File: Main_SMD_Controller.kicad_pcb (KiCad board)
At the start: 4 copper layers, 65 x 85 mm, 59 parts, among them J1 2.1-5.5 +12VDC, J10 Vin_-, J11 Conn_01x02, J12 Vsens, J13 Vin+, J2 Switch_Control, J3 +5V, J4 AnalogIO, J5 +12V, J6 VsensJMP, J7 Drain, J8 Gate, J9 Source, P1 Eoshi-chan_Silk, P2 Eoshi-chan_Silk, P3 Serial_QR, Q1 2N7002K, U1 NJW4191M, U2 NJM7805SDL1, U3 TC74HC4066AP, U4 AD8226ARZ, U5 S-89713B-K8T2U

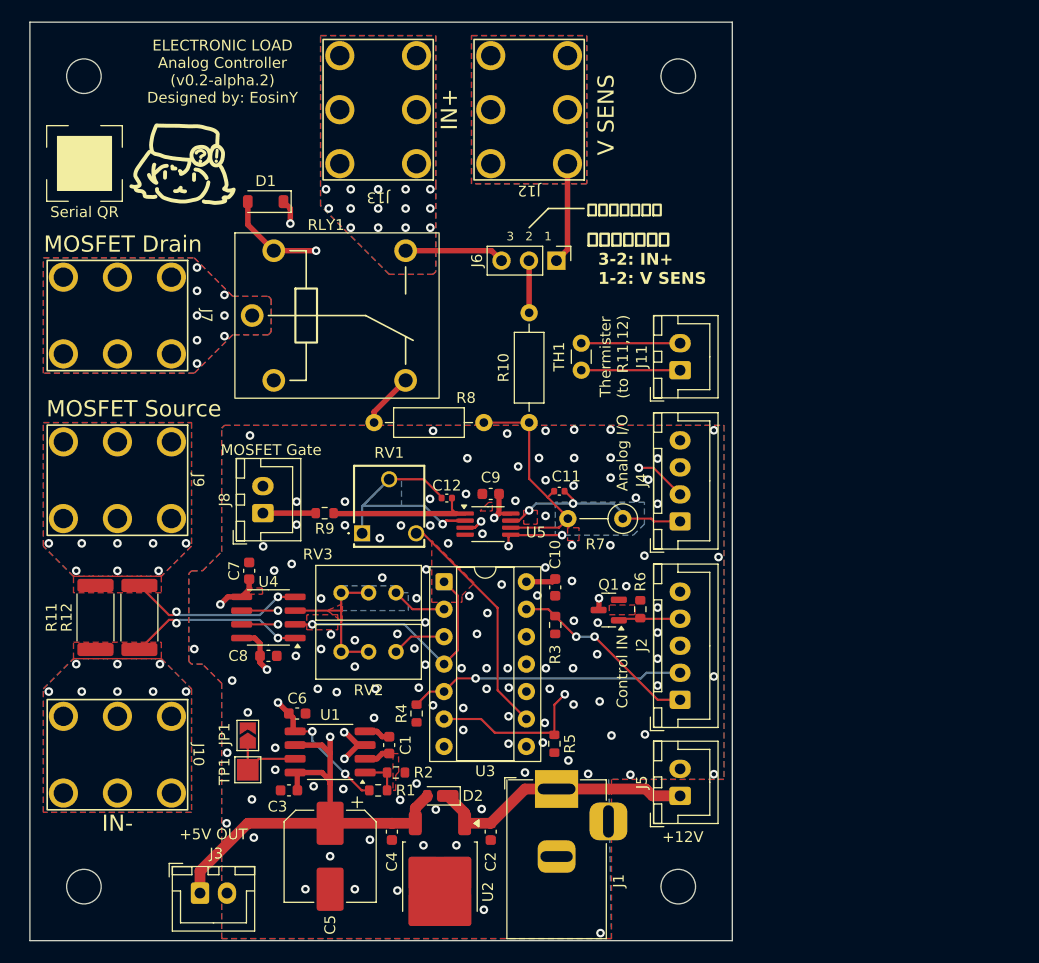
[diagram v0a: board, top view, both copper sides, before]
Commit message: 4 layered
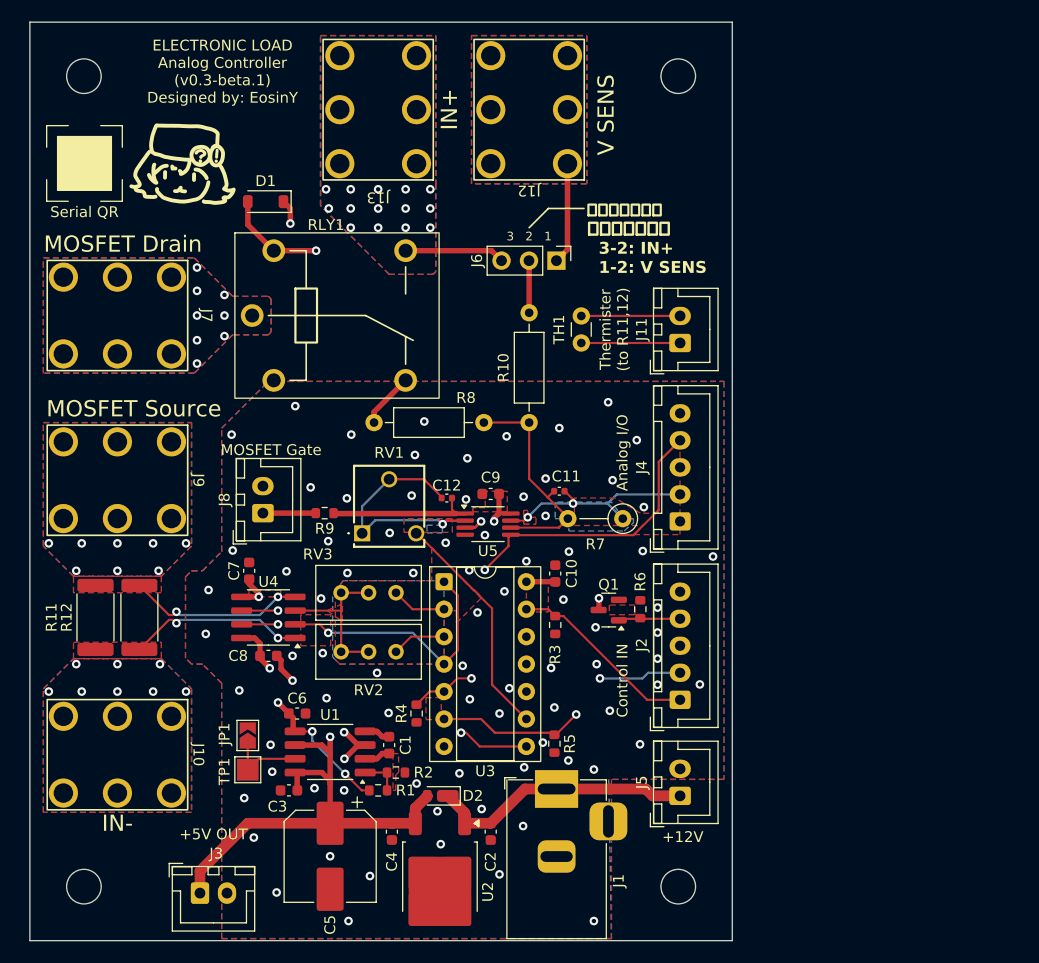
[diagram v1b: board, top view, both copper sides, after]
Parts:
- J4: footprint Connector_JST:JST_XH_B4B-XH-A_1x04_P2.50mm_Vertical -> Connector_JST:JST_XH_B5B-XH-A_1x05_P2.50mm_Vertical
- moved J11 2.52 mm to (90.2, 59.7)
- moved TH1 2.52 mm to (81.0, 59.7)
- moved C10 1.28 mm to (78.6, 81.0), turned to 90 degrees
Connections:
- J4 pad 1: /Vmeas -> /Imeas
- J4 pad 2: /Vref -> /Vmeas
- J4 pad 3: Vofs -> /Vref
- J4 pad 4: GND -> Vofs
- U3 pad 8: Net-(U3-Pad8) -> /Imeas
- U4 pad 7: Net-(U3-Pad8) -> /Imeas
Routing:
- net /Imeas: track 0.00 -> 72.2 mm, vias 0 -> 2
- net Net-(U3-Pad8): track 31.0 -> 0.00 mm, vias 1 -> 0
- net R-: track 52.3 -> 48.9 mm
- net GND: track 4.24 -> 7.13 mm, vias 123 -> 84
- net Vofs: track 47.7 -> 50.2 mm, vias 3 -> 2
- net Vconst_ENABLE: track 27.4 -> 25.8 mm
- net /Vmeas: track 19.0 -> 20.4 mm
- net VEE: track 28.3 -> 26.9 mm
- net /Vref: track 23.4 -> 22.2 mm, vias 2 -> 1
- net SHUNT_SELECT1: vias 1 -> 2
- net SHUNT_SELECT2: vias 2 -> 0
- added copper zone on In1.Cu, net GND
- added copper zone on In2.Cu, net GND
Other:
- board text added: "ELECTRONIC LOAD Analog Controller (v0.3-beta.1) Designed by: EosinY"
- board text removed: "ELECTRONIC LOAD Analog Controller (v0.2-alpha.2) Designed by: EosinY"

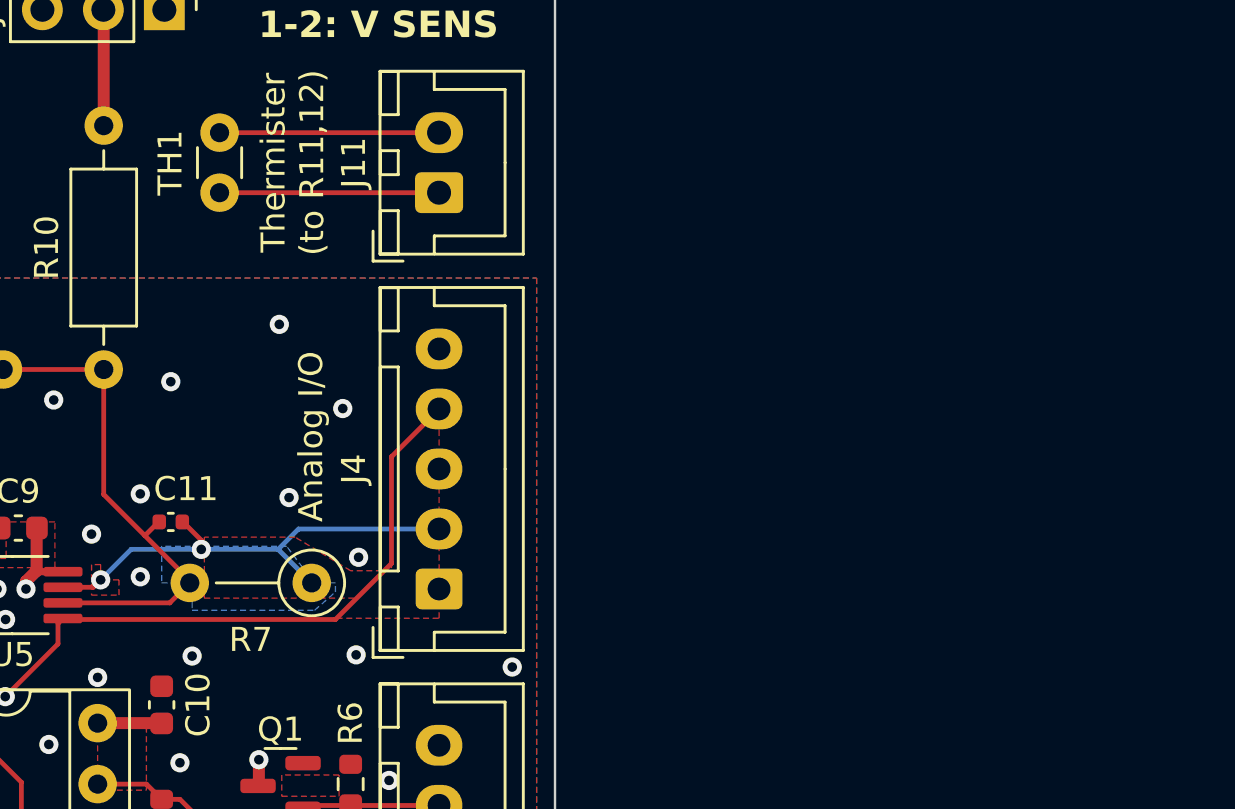
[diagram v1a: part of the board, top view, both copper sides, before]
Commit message: fix voltage measure circuit
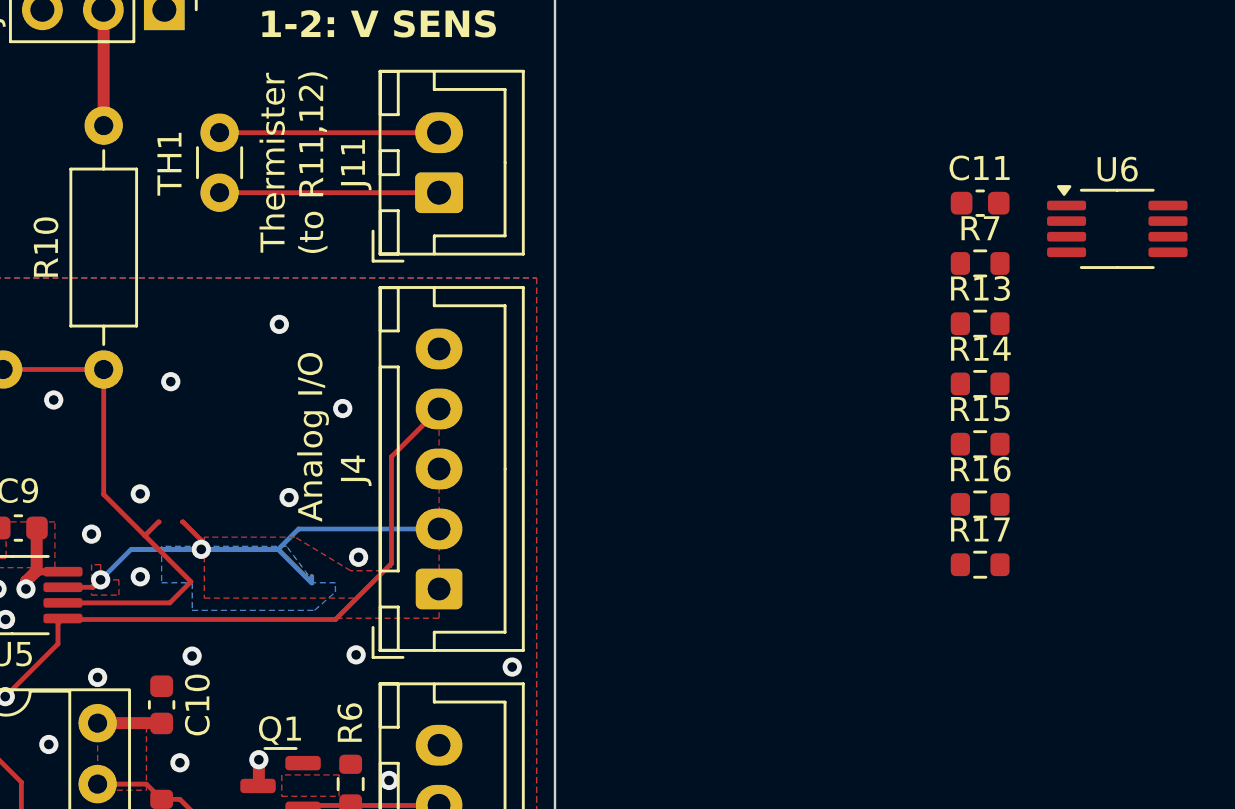
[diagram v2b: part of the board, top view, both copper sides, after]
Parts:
- added R13: 10k, Resistor_SMD:R_0603_1608Metric, F.Cu at (112.7, 65.1)
- added R14: 10k, Resistor_SMD:R_0603_1608Metric, F.Cu at (112.7, 67.7)
- added R15: 10k, Resistor_SMD:R_0603_1608Metric, F.Cu at (112.7, 70.2)
- added R16: 10k, Resistor_SMD:R_0603_1608Metric, F.Cu at (112.7, 72.7)
- added R17: 10k, Resistor_SMD:R_0603_1608Metric, F.Cu at (112.7, 75.2)
- added U6: S-89713B-K8T2U, Package_SO:MSOP-8_3x3mm_P0.65mm, F.Cu at (118.4, 61.2)
- C11: value 0.01u -> 0.1u; footprint Capacitor_SMD:C_0402_1005Metric -> Capacitor_SMD:C_0603_1608Metric
- R10: value 390k -> 150k
- R7: value 390k -> 10k; footprint Resistor_THT:R_Axial_DIN0207_L6.3mm_D2.5mm_P5.08mm_Vertical -> Resistor_SMD:R_0603_1608Metric
- moved C11 36.2 mm to (112.7, 60.1), turned to 0 degrees
- moved R7 30.9 mm to (112.7, 62.6), turned to 0 degrees
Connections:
- C11 pad 1: /Vmeas -> VCC
- C11 pad 2: Net-(C11-Pad2) -> GND
- R10 pad 1: Net-(C11-Pad2) -> Net-(R10-Pad1)
- R7 pad 1: /Vmeas -> Net-(R17-Pad2)
- R7 pad 2: Net-(C11-Pad2) -> VCC
- R8 pad 2: Net-(C11-Pad2) -> Net-(R10-Pad1)
- U5 pad 5: Vofs -> Net-(R10-Pad1)
- U5 pad 6: Net-(C11-Pad2) -> Net-(R13-Pad2)
- U5 pad 7: /Vmeas -> Net-(R13-Pad2)
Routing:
- net Net-(C11-Pad2): track 21.1 -> 0.00 mm
- net (no net): track 0.00 -> 21.1 mm

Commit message: 1733
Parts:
- moved U6 40.7 mm to (80.7, 76.4)
- moved R13 38.8 mm to (75.8, 77.1), turned to 180 degrees
- moved R15 36.4 mm to (76.6, 74.8), turned to 90 degrees
- moved R7 35.3 mm to (81.5, 79.0), turned to 180 degrees
- moved R16 33.6 mm to (79.1, 73.8)
- moved C11 32.1 mm to (85.0, 76.3), turned to -90 degrees
- moved R14 30.9 mm to (82.4, 73.8)
- moved R17 28.4 mm to (84.6, 79.0), turned to 180 degrees
- moved U5 1.55 mm to (70.8, 76.5)
- moved C9 0.16 mm to (72.5, 73.6)
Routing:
- net (no net): track 21.1 -> 0.00 mm
- net VCC: track 98.9 -> 116.1 mm
- net /Vmeas: track 20.4 -> 12.7 mm, vias 2 -> 1
- net Net-(R13-Pad1): track 0.00 -> 6.81 mm
- net Net-(R15-Pad1): track 0.00 -> 5.36 mm
- net Net-(R10-Pad1): track 0.00 -> 4.19 mm
- net Net-(R17-Pad2): track 0.00 -> 3.22 mm
- net Net-(R13-Pad2): track 0.00 -> 2.81 mm
- net GND: track 7.13 -> 9.20 mm, vias 84 -> 78
- net Net-(C12-Pad1): track 22.0 -> 20.1 mm
- net /Vref: track 22.2 -> 23.9 mm
- net Vofs: track 50.2 -> 48.6 mm
- net Net-(C12-Pad2): track 13.8 -> 12.2 mm
- net Net-(U6-Pad6): track 0.00 -> 0.65 mm

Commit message: bom and schematic pdf
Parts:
- added C13: 1u, Capacitor_SMD:C_0603_1608Metric, F.Cu at (50.2, 92.5)
- added R18: 10k, Resistor_SMD:R_0603_1608Metric, F.Cu at (53.2, 92.5)
- moved R17 2.41 mm to (82.7, 80.5)
- moved C11 1.48 mm to (83.5, 76.7)
- moved C12 1.45 mm to (67.2, 73.7), turned to -90 degrees
- moved R14 1.40 mm to (81.0, 73.9)
- moved R16 1.40 mm to (77.7, 73.9)
- moved U6 1.22 mm to (79.5, 76.5)
- moved R15 1.17 mm to (75.4, 74.9)
- moved C9 1.16 mm to (71.4, 73.9)
- moved RV1 1.10 mm to (59.7, 77.7)
- moved R13 1.10 mm to (74.7, 77.2)
- moved U5 0.91 mm to (69.9, 76.5)
- moved R9 0.89 mm to (56.4, 75.4)
- moved J8 0.76 mm to (50.8, 75.4)
- moved R7 0.46 mm to (81.0, 79.0)
- moved C6 0.13 mm to (54.9, 94.0)
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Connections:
- C6 pad 1: VEE -> Net-(U1-Vout)
- R1 pad 2: VEE -> Net-(U1-Vout)
- U1 pad 5: VEE -> Net-(U1-Vout)
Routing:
- net Net-(U1-Vout): track 0.00 -> 13.1 mm, vias 0 -> 2
- net Net-(R10-Pad1): track 4.19 -> 17.1 mm, vias 0 -> 1
- net VEE: track 26.9 -> 14.4 mm, vias 4 -> 2
- net VCC: track 116.1 -> 109.6 mm
- net R-: track 48.9 -> 53.0 mm, vias 10 -> 14
- net /Vmeas: track 12.7 -> 15.6 mm
- net /Vref: track 23.9 -> 26.5 mm
- net Vofs: track 48.6 -> 50.7 mm
- net GND: track 9.20 -> 7.13 mm, vias 78 -> 87
- net Net-(RV1-Pad3): track 21.5 -> 22.3 mm
- net SHUNT_SELECT1: vias 2 -> 1
- net /R+: vias 10 -> 14
- net /MOS+: vias 8 -> 12
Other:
- board text added: "ELECTRONIC LOAD Analog Controller (v0.4-beta.1) Designed by: EosinY"
- board text removed: "ELECTRONIC LOAD Analog Controller (v0.3-beta.1) Designed by: EosinY"
